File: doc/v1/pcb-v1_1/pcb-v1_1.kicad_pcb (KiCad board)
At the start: 2 copper layers, 65 x 145 mm, 146 parts, among them P1 Raspberry_Pi_2_3, P10 CONN_01X04, P11 CONN_01X03, P12 CONN_01X03, P13 CONN_01X03, P14 CONN_01X03, P15 CONN_01X03, P2 CONN_02X08, P3 CONN_02X04, P4 CONN_02X04, P5 CONN_01X04, P6 CONN_01X03, P7 CONN_01X03, P8 CONN_01X03, P9 CONN_01X04, Q1 BC547, Q2 BC547, Q3 BC547, U1 MCP3008, U2 74LS08, U3 MCP23017, U4 MCP23017

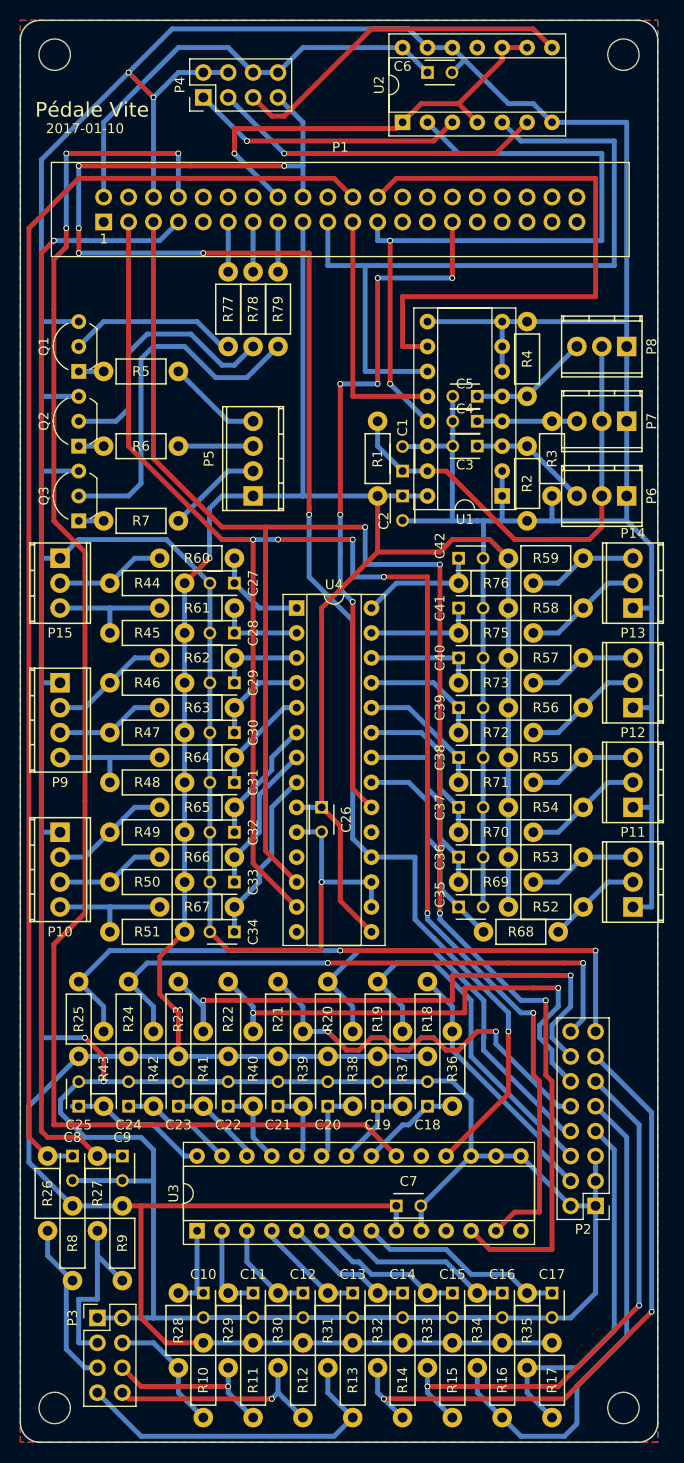
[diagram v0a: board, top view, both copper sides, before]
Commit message: Updated board files to KiCAD 6
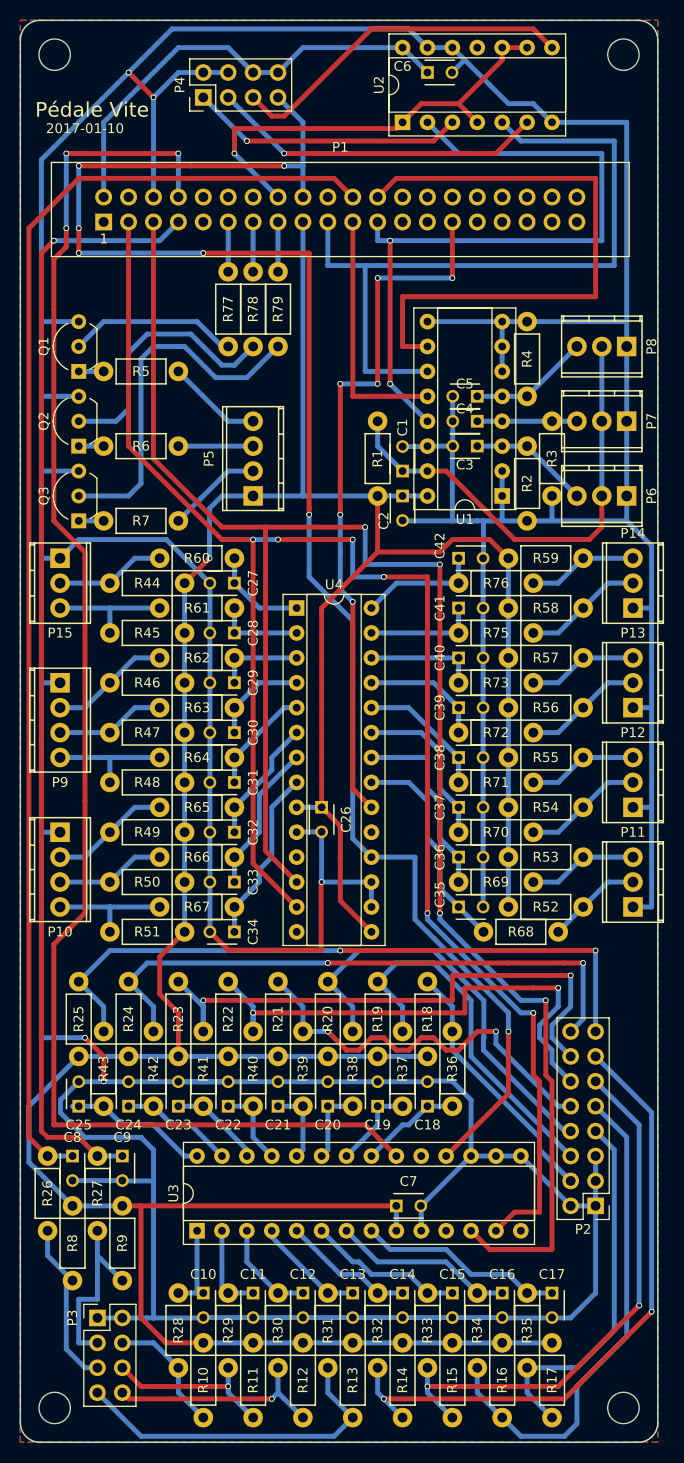
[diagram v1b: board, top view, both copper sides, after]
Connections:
- net ~Disp_CS renamed ~{Disp_CS}
- net ~Reset renamed ~{Reset}
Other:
- net class Default removed
- net class Standard removed
